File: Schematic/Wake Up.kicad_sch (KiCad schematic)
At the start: 13 parts, among them Q14 BSS123, Q15 ZXMP10A13F, Q16 BSS123

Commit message: added sensors?
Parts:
- renumbered Q14 to Q18, Q15 to Q19, Q16 to Q20

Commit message: 1st Schematic Review
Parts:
- renumbered C23 to C26, R55 to R57, R56 to R58, R57 to R59, R58 to R60, R59 to R61, R60 to R62
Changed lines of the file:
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@@
 		(on_board yes)
 		(dnp no)
-		(property "Reference" "#PWR019"
+		(property "Reference" "#PWR024"
 			(at 156.21 114.3 0)
 			(effects
@@
 			(project "STAR"
 				(path "/fc8533bc-25dd-4c20-9b4c-ffebebd6739b/e8da5d81-614b-4fe5-84b3-4c351fab7114/9d9414eb-0fa9-444a-a653-4c48988997ba"
-					(reference "#PWR019")
+					(reference "#PWR024")
 					(unit 1)
 				)
@@
 		(on_board yes)
 		(dnp no)
-		(property "Reference" "R58"
+		(property "Reference" "R60"
 			(at 158.242 82.804 0)
 			(effects
@@
 			(project "STAR"
 				(path "/fc8533bc-25dd-4c20-9b4c-ffebebd6739b/e8da5d81-614b-4fe5-84b3-4c351fab7114/9d9414eb-0fa9-444a-a653-4c48988997ba"
-					(reference "R58")
+					(reference "R60")
 					(unit 1)
 				)
@@
 		(on_board yes)
 		(dnp no)
-		(property "Reference" "#PWR020"
+		(property "Reference" "#PWR025"
 			(at 186.69 95.25 0)
 			(effects
@@
 			(project "STAR"
 				(path "/fc8533bc-25dd-4c20-9b4c-ffebebd6739b/e8da5d81-614b-4fe5-84b3-4c351fab7114/9d9414eb-0fa9-444a-a653-4c48988997ba"
-					(reference "#PWR020")
+					(reference "#PWR025")
 					(unit 1)
 				)
@@
 		(on_board yes)
 		(dnp no)
-		(property "Reference" "R55"
+		(property "Reference" "R57"
 			(at 136.652 62.484 0)
 			(effects
@@
 			(project "STAR"
 				(path "/fc8533bc-25dd-4c20-9b4c-ffebebd6739b/e8da5d81-614b-4fe5-84b3-4c351fab7114/9d9414eb-0fa9-444a-a653-4c48988997ba"
-					(reference "R55")
+					(reference "R57")
 					(unit 1)
 				)
@@
 		(on_board yes)
 		(dnp no)
-		(property "Reference" "R56"
+		(property "Reference" "R58"
 			(at 139.192 101.854 0)
 			(effects
@@
 			(project "STAR"
 				(path "/fc8533bc-25dd-4c20-9b4c-ffebebd6739b/e8da5d81-614b-4fe5-84b3-4c351fab7114/9d9414eb-0fa9-444a-a653-4c48988997ba"
-					(reference "R56")
+					(reference "R58")
 					(unit 1)
 				)
@@
 		(on_board yes)
 		(dnp no)
-		(property "Reference" "#PWR018"
+		(property "Reference" "#PWR023"
 			(at 143.51 134.62 0)
 			(effects
@@
 			(project "STAR"
 				(path "/fc8533bc-25dd-4c20-9b4c-ffebebd6739b/e8da5d81-614b-4fe5-84b3-4c351fab7114/9d9414eb-0fa9-444a-a653-4c48988997ba"
-					(reference "#PWR018")
+					(reference "#PWR023")
 					(unit 1)
 				)
@@
 		(on_board yes)
 		(dnp no)
-		(property "Reference" "C23"
+		(property "Reference" "C26"
 			(at 124.46 71.374 90)
 			(effects
@@
 			(project "STAR"
 				(path "/fc8533bc-25dd-4c20-9b4c-ffebebd6739b/e8da5d81-614b-4fe5-84b3-4c351fab7114/9d9414eb-0fa9-444a-a653-4c48988997ba"
-					(reference "C23")
+					(reference "C26")
 					(unit 1)
 				)
@@
 		(on_board yes)
 		(dnp no)
-		(property "Reference" "R57"
+		(property "Reference" "R59"
 			(at 145.542 101.854 0)
 			(effects
@@
 			(project "STAR"
 				(path "/fc8533bc-25dd-4c20-9b4c-ffebebd6739b/e8da5d81-614b-4fe5-84b3-4c351fab7114/9d9414eb-0fa9-444a-a653-4c48988997ba"
-					(reference "R57")
+					(reference "R59")
 					(unit 1)
 				)
@@
 		(on_board yes)
 		(dnp no)
-		(property "Reference" "R59"
+		(property "Reference" "R61"
 			(at 158.242 99.314 0)
 			(effects
@@
 			(project "STAR"
 				(path "/fc8533bc-25dd-4c20-9b4c-ffebebd6739b/e8da5d81-614b-4fe5-84b3-4c351fab7114/9d9414eb-0fa9-444a-a653-4c48988997ba"
-					(reference "R59")
+					(reference "R61")
 					(unit 1)
 				)
@@
 		(on_board yes)
 		(dnp no)
-		(property "Reference" "R60"
+		(property "Reference" "R62"
 			(at 170.942 105.664 0)
 			(effects
@@
 			(project "STAR"
 				(path "/fc8533bc-25dd-4c20-9b4c-ffebebd6739b/e8da5d81-614b-4fe5-84b3-4c351fab7114/9d9414eb-0fa9-444a-a653-4c48988997ba"
-					(reference "R60")
+					(reference "R62")
 					(unit 1)
 				)

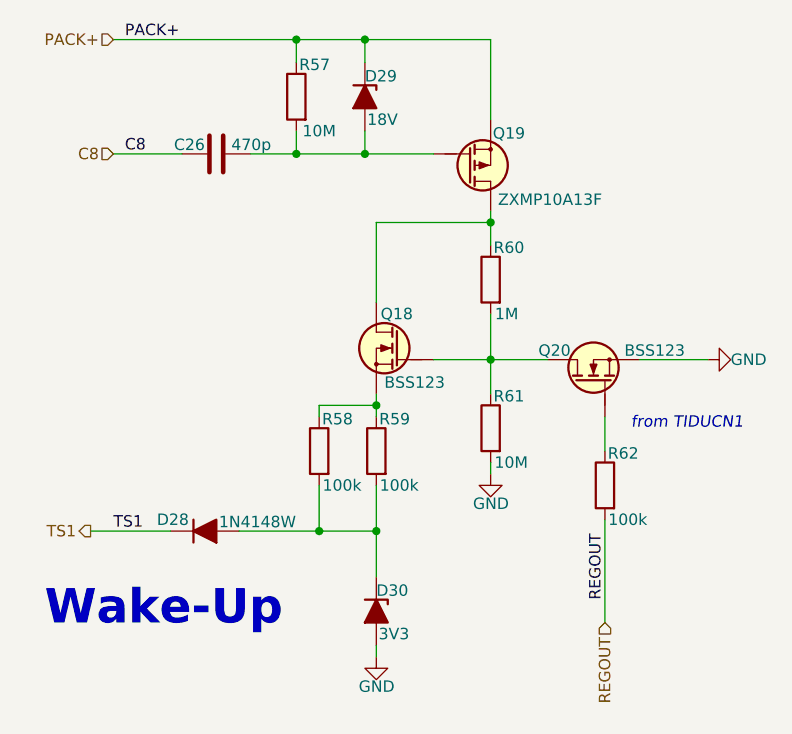
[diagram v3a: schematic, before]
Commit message: Added MCU
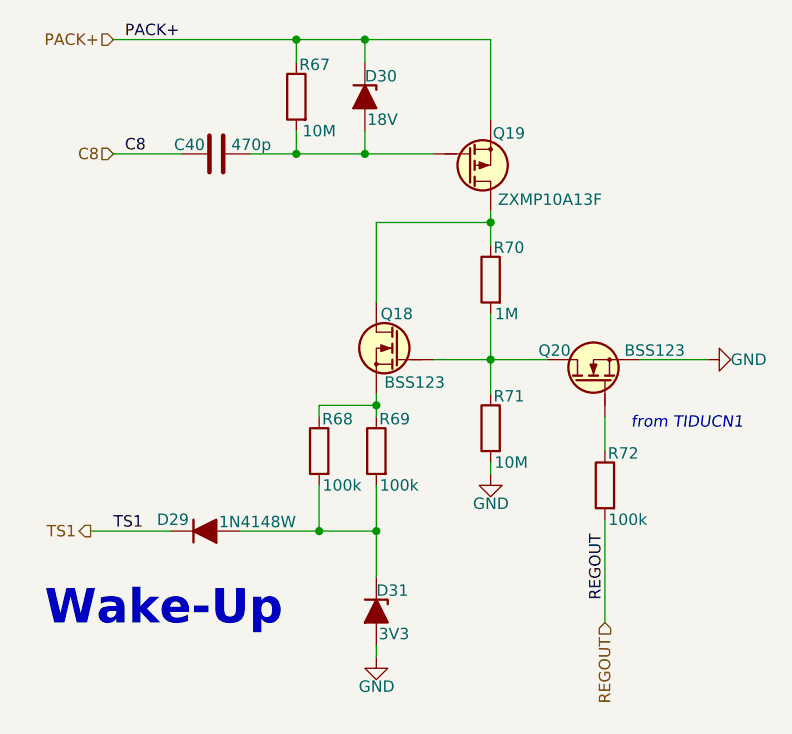
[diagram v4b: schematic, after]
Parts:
- renumbered C26 to C40, D28 to D29, D29 to D30, D30 to D31, R57 to R67, R58 to R68, R59 to R69, R60 to R70, R61 to R71, R62 to R72
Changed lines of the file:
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@@
 		(on_board yes)
 		(dnp no)
-		(property "Reference" "#PWR025"
+		(property "Reference" "#PWR034"
 			(at 156.21 114.3 0)
 			(effects
@@
 			(project "STAR"
 				(path "/fc8533bc-25dd-4c20-9b4c-ffebebd6739b/e8da5d81-614b-4fe5-84b3-4c351fab7114/9d9414eb-0fa9-444a-a653-4c48988997ba"
-					(reference "#PWR025")
+					(reference "#PWR034")
 					(unit 1)
 				)
@@
 		(on_board yes)
 		(dnp no)
-		(property "Reference" "D30"
+		(property "Reference" "D31"
 			(at 143.51 120.904 90)
 			(effects
@@
 			(project "STAR"
 				(path "/fc8533bc-25dd-4c20-9b4c-ffebebd6739b/e8da5d81-614b-4fe5-84b3-4c351fab7114/9d9414eb-0fa9-444a-a653-4c48988997ba"
-					(reference "D30")
+					(reference "D31")
 					(unit 1)
 				)
@@
 		(on_board yes)
 		(dnp no)
-		(property "Reference" "R60"
+		(property "Reference" "R70"
 			(at 158.242 82.804 0)
 			(effects
@@
 			(project "STAR"
 				(path "/fc8533bc-25dd-4c20-9b4c-ffebebd6739b/e8da5d81-614b-4fe5-84b3-4c351fab7114/9d9414eb-0fa9-444a-a653-4c48988997ba"
-					(reference "R60")
+					(reference "R70")
 					(unit 1)
 				)
@@
 		(on_board yes)
 		(dnp no)
-		(property "Reference" "#PWR026"
+		(property "Reference" "#PWR035"
 			(at 186.69 95.25 0)
 			(effects
@@
 			(project "STAR"
 				(path "/fc8533bc-25dd-4c20-9b4c-ffebebd6739b/e8da5d81-614b-4fe5-84b3-4c351fab7114/9d9414eb-0fa9-444a-a653-4c48988997ba"
-					(reference "#PWR026")
+					(reference "#PWR035")
 					(unit 1)
 				)
@@
 		(on_board yes)
 		(dnp no)
-		(property "Reference" "R57"
+		(property "Reference" "R67"
 			(at 136.652 62.484 0)
 			(effects
@@
 			(project "STAR"
 				(path "/fc8533bc-25dd-4c20-9b4c-ffebebd6739b/e8da5d81-614b-4fe5-84b3-4c351fab7114/9d9414eb-0fa9-444a-a653-4c48988997ba"
-					(reference "R57")
+					(reference "R67")
 					(unit 1)
 				)
@@
 		(on_board yes)
 		(dnp no)
-		(property "Reference" "R58"
+		(property "Reference" "R68"
 			(at 139.192 101.854 0)
 			(effects
@@
 			(project "STAR"
 				(path "/fc8533bc-25dd-4c20-9b4c-ffebebd6739b/e8da5d81-614b-4fe5-84b3-4c351fab7114/9d9414eb-0fa9-444a-a653-4c48988997ba"
-					(reference "R58")
+					(reference "R68")
 					(unit 1)
 				)
@@
 		(on_board yes)
 		(dnp no)
-		(property "Reference" "#PWR024"
+		(property "Reference" "#PWR033"
 			(at 143.51 134.62 0)
 			(effects
@@
 			(project "STAR"
 				(path "/fc8533bc-25dd-4c20-9b4c-ffebebd6739b/e8da5d81-614b-4fe5-84b3-4c351fab7114/9d9414eb-0fa9-444a-a653-4c48988997ba"
-					(reference "#PWR024")
+					(reference "#PWR033")
 					(unit 1)
 				)
@@
 		(on_board yes)
 		(dnp no)
-		(property "Reference" "C26"
+		(property "Reference" "C40"
 			(at 124.46 71.374 90)
 			(effects
@@
 			(project "STAR"
 				(path "/fc8533bc-25dd-4c20-9b4c-ffebebd6739b/e8da5d81-614b-4fe5-84b3-4c351fab7114/9d9414eb-0fa9-444a-a653-4c48988997ba"
-					(reference "C26")
+					(reference "C40")
 					(unit 1)
 				)
@@
 		(on_board yes)
 		(dnp no)
-		(property "Reference" "D28"
+		(property "Reference" "D29"
 			(at 120.904 113.03 0)
 			(effects
@@
 			(project "STAR"
 				(path "/fc8533bc-25dd-4c20-9b4c-ffebebd6739b/e8da5d81-614b-4fe5-84b3-4c351fab7114/9d9414eb-0fa9-444a-a653-4c48988997ba"
-					(reference "D28")
+					(reference "D29")
 					(unit 1)
 				)
@@
 		(on_board yes)
 		(dnp no)
-		(property "Reference" "R59"
+		(property "Reference" "R69"
 			(at 145.542 101.854 0)
 			(effects
@@
 			(project "STAR"
 				(path "/fc8533bc-25dd-4c20-9b4c-ffebebd6739b/e8da5d81-614b-4fe5-84b3-4c351fab7114/9d9414eb-0fa9-444a-a653-4c48988997ba"
-					(reference "R59")
+					(reference "R69")
 					(unit 1)
 				)
@@
 		(on_board yes)
 		(dnp no)
-		(property "Reference" "D29"
+		(property "Reference" "D30"
 			(at 142.24 63.754 90)
 			(effects
@@
 			(project "STAR"
 				(path "/fc8533bc-25dd-4c20-9b4c-ffebebd6739b/e8da5d81-614b-4fe5-84b3-4c351fab7114/9d9414eb-0fa9-444a-a653-4c48988997ba"
-					(reference "D29")
+					(reference "D30")
 					(unit 1)
 				)
@@
 		(on_board yes)
 		(dnp no)
-		(property "Reference" "R61"
+		(property "Reference" "R71"
 			(at 158.242 99.314 0)
 			(effects
@@
 			(project "STAR"
 				(path "/fc8533bc-25dd-4c20-9b4c-ffebebd6739b/e8da5d81-614b-4fe5-84b3-4c351fab7114/9d9414eb-0fa9-444a-a653-4c48988997ba"
-					(reference "R61")
+					(reference "R71")
 					(unit 1)
 				)
@@
 		(on_board yes)
 		(dnp no)
-		(property "Reference" "R62"
+		(property "Reference" "R72"
 			(at 170.942 105.664 0)
 			(effects
@@
 			(project "STAR"
 				(path "/fc8533bc-25dd-4c20-9b4c-ffebebd6739b/e8da5d81-614b-4fe5-84b3-4c351fab7114/9d9414eb-0fa9-444a-a653-4c48988997ba"
-					(reference "R62")
+					(reference "R72")
 					(unit 1)
 				)

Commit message: Started to work on the BOM
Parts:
- C35: renamed from C40; footprint (none) -> Capacitor_SMD:C_0603_1608Metric_Pad1.08x0.95mm_HandSolder; Link (none) -> https://mou.sr/3UXYSz1; Manufacturer Part Number (none) -> CL10C471JB8NNND; Price per Unit (none) -> 0.10; Supplier (none) -> Mouser; Supplier Part Number (none) -> 187-CL10C471JB8NNND
- D26: renamed from D29; footprint PCM_Diode_SMD_AKL:D_SOD-123 -> 1N4148W:SODFL3816X120N; Link (none) -> https://mou.sr/3kOR7fV; Manufacturer Part Number (none) -> 1N4148W; Price per Unit (none) -> 0.10; Supplier (none) -> Mouser; Supplier Part Number (none) -> 637-1N4148W
- D27: renamed from D30; footprint (none) -> MMSZ3V9T1G:SOD3716X135N; Link (none) -> https://mou.sr/46cbcRl; Manufacturer Part Number (none) -> MMSZ4705-E3-08; Price per Unit (none) -> 0.10; Supplier (none) -> Mouser; Supplier Part Number (none) -> 78-MMSZ4705-E3-08
- D28: renamed from D31; value 3V3 -> 3V9; footprint (none) -> MMSZ3V9T1G:SOD3716X135N; Link (none) -> https://mou.sr/3JLnhp2; Manufacturer Part Number (none) -> MMSZ3V9T1G; Price per Unit (none) -> 0.10; Supplier (none) -> Mouser; Supplier Part Number (none) -> 863-MMSZ3V9T1G
- Q18, Q19, Q20: footprint PCM_Package_TO_SOT_SMD_AKL:SOT-23 -> (none)
- renumbered R67 to R63, R68 to R64, R69 to R65, R70 to R66, R71 to R67, R72 to R68

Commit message: Massive pivit, simplification
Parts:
- renumbered C35 to C28, D26 to D25, D27 to D26, D28 to D27
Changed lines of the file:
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@@
 		(on_board yes)
 		(dnp no)
-		(property "Reference" "#PWR029"
+		(property "Reference" "#PWR018"
 			(at 156.21 114.3 0)
 			(effects
@@
 			(project "STAR"
 				(path "/fc8533bc-25dd-4c20-9b4c-ffebebd6739b/e8da5d81-614b-4fe5-84b3-4c351fab7114/9d9414eb-0fa9-444a-a653-4c48988997ba"
-					(reference "#PWR029")
+					(reference "#PWR018")
 					(unit 1)
 				)
@@
 		(on_board yes)
 		(dnp no)
-		(property "Reference" "D28"
+		(property "Reference" "D27"
 			(at 143.51 120.904 90)
 			(effects
@@
 			)
 		)
+		(property "SNAPEDA_PACKAGE_ID" ""
+			(at 143.51 123.19 90)
+			(effects
+				(font
+					(size 1.27 1.27)
+				)
+				(hide yes)
+			)
+		)
 		(pin "2"
 		)
@@
 			(project "STAR"
 				(path "/fc8533bc-25dd-4c20-9b4c-ffebebd6739b/e8da5d81-614b-4fe5-84b3-4c351fab7114/9d9414eb-0fa9-444a-a653-4c48988997ba"
-					(reference "D28")
+					(reference "D27")
 					(unit 1)
 				)
@@
 			)
 		)
+		(property "SNAPEDA_PACKAGE_ID" ""
+			(at 156.21 86.36 0)
+			(effects
+				(font
+					(size 1.27 1.27)
+				)
+				(hide yes)
+			)
+		)
 		(pin "1"
 		)
@@
 		(on_board yes)
 		(dnp no)
-		(property "Reference" "#PWR030"
+		(property "Reference" "#PWR019"
 			(at 186.69 95.25 0)
 			(effects
@@
 			(project "STAR"
 				(path "/fc8533bc-25dd-4c20-9b4c-ffebebd6739b/e8da5d81-614b-4fe5-84b3-4c351fab7114/9d9414eb-0fa9-444a-a653-4c48988997ba"
-					(reference "#PWR030")
+					(reference "#PWR019")
 					(unit 1)
 				)
@@
 			)
 		)
+		(property "SNAPEDA_PACKAGE_ID" ""
+			(at 134.62 66.04 0)
+			(effects
+				(font
+					(size 1.27 1.27)
+				)
+				(hide yes)
+			)
+		)
 		(pin "1"
 		)
@@
 			)
 		)
+		(property "SNAPEDA_PACKAGE_ID" ""
+			(at 137.16 105.41 0)
+			(effects
+				(font
+					(size 1.27 1.27)
+				)
+				(hide yes)
+			)
+		)
 		(pin "1"
 		)
@@
 		(on_board yes)
 		(dnp no)
-		(property "Reference" "#PWR028"
+		(property "Reference" "#PWR017"
 			(at 143.51 134.62 0)
 			(effects
@@
 			(project "STAR"
 				(path "/fc8533bc-25dd-4c20-9b4c-ffebebd6739b/e8da5d81-614b-4fe5-84b3-4c351fab7114/9d9414eb-0fa9-444a-a653-4c48988997ba"
-					(reference "#PWR028")
+					(reference "#PWR017")
 					(unit 1)
 				)
@@
 			)
 		)
+		(property "SNAPEDA_PACKAGE_ID" ""
+			(at 153.67 73.66 0)
+			(effects
+				(font
+					(size 1.27 1.27)
+				)
+				(hide yes)
+			)
+		)
 		(pin "3"
 		)
@@
 			)
 		)
+		(property "SNAPEDA_PACKAGE_ID" ""
+			(at 167.64 97.79 90)
+			(effects
+				(font
+					(size 1.27 1.27)
+				)
+				(hide yes)
+			)
+		)
 		(pin "1"
 		)
@@
 		(on_board yes)
 		(dnp no)
-		(property "Reference" "C35"
+		(property "Reference" "C28"
 			(at 124.46 71.374 90)
 			(effects
@@
 			)
 		)
+		(property "SNAPEDA_PACKAGE_ID" ""
+			(at 125.73 72.39 90)
+			(effects
+				(font
+					(size 1.27 1.27)
+				)
+				(hide yes)
+			)
+		)
 		(pin "1"
 		)
@@
 			(project "STAR"
 				(path "/fc8533bc-25dd-4c20-9b4c-ffebebd6739b/e8da5d81-614b-4fe5-84b3-4c351fab7114/9d9414eb-0fa9-444a-a653-4c48988997ba"
-					(reference "C35")
+					(reference "C28")
 					(unit 1)
 				)
@@
 		(on_board yes)
 		(dnp no)
-		(property "Reference" "D26"
+		(property "Reference" "D25"
 			(at 120.904 113.03 0)
 			(effects
@@
 			)
 		)
+		(property "SNAPEDA_PACKAGE_ID" ""
+			(at 124.46 114.3 0)
+			(effects
+				(font
+					(size 1.27 1.27)
+				)
+				(hide yes)
+			)
+		)
 		(pin "2"
 		)
@@
 			(project "STAR"
 				(path "/fc8533bc-25dd-4c20-9b4c-ffebebd6739b/e8da5d81-614b-4fe5-84b3-4c351fab7114/9d9414eb-0fa9-444a-a653-4c48988997ba"
-					(reference "D26")
+					(reference "D25")
 					(unit 1)
 				)
@@
 			)
 		)
+		(property "SNAPEDA_PACKAGE_ID" ""
+			(at 143.51 105.41 0)
+			(effects
+				(font
+					(size 1.27 1.27)
+				)
+				(hide yes)
+			)
+		)
 		(pin "1"
 		)
@@
 		(on_board yes)
 		(dnp no)
-		(property "Reference" "D27"
+		(property "Reference" "D26"
 			(at 142.24 63.754 90)
 			(effects
@@
 			)
 		)
+		(property "SNAPEDA_PACKAGE_ID" ""
+			(at 142.24 66.04 90)
+			(effects
+				(font
+					(size 1.27 1.27)
+				)
+				(hide yes)
+			)
+		)
 		(pin "2"
 		)
@@
 			(project "STAR"
 				(path "/fc8533bc-25dd-4c20-9b4c-ffebebd6739b/e8da5d81-614b-4fe5-84b3-4c351fab7114/9d9414eb-0fa9-444a-a653-4c48988997ba"
-					(reference "D27")
+					(reference "D26")
 					(unit 1)
 				)
@@
 			)
 		)
+		(property "SNAPEDA_PACKAGE_ID" ""
+			(at 146.05 93.98 0)
+			(effects
+				(font
+					(size 1.27 1.27)
+				)
+				(hide yes)
+			)
+		)
 		(pin "1"
 		)
@@
 			)
 		)
+		(property "SNAPEDA_PACKAGE_ID" ""
+			(at 156.21 102.87 0)
+			(effects
+				(font
+					(size 1.27 1.27)
+				)
+				(hide yes)
+			)
+		)
 		(pin "1"
 		)
@@
 			(at 168.91 109.22 0)
 			(effects
+				(font
+					(size 1.27 1.27)
+				)
+				(hide yes)
+			)
+		)
+		(property "SNAPEDA_PACKAGE_ID" ""
+			(at 168.91 109.22 0)
+			(effects
